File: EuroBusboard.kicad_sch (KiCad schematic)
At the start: 24 parts, among them J1 Power In, J10 IDC5, J11 JST5, J12 IDC6, J13 JST6, J14 IDC7, J15 JST7, J16 IDC8, J17 JST8, J18 Power thru, J2 IDC1, J3 JST1, J4 IDC2, J5 JST2, J6 IDC3, J7 JST3, J8 IDC4, J9 JST4

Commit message: Schematic rev0.1 update
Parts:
- added D3, D4: 4007, symbol Device:D
- added H1, H2, H3, H4: MountingHole_Pad, symbol Mechanical:MountingHole_Pad
- added J19: Power In, symbol DIYSynthMNL:JST_Eurorack_power_3P
- added J20: Power thru, symbol DIYSynthMNL:JST_Eurorack_power_3P
- added TP1: +12V, symbol Connector:TestPoint
- added TP2: GND, symbol Connector:TestPoint
- added TP3: -12V, symbol Connector:TestPoint
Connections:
- net +12V: now also D3.1 (K), J20.1 (+12v), TP1.1; no longer J1.1 (Pin_1)
- net -12V: now also D4.2 (A), J20.3 (-12v), TP3.1; no longer J1.3 (Pin_3)
- net GND: now also H1.1, H2.1, H3.1, H4.1, J19.2 (GND), J20.2 (GND), TP2.1
- new net +12V_IN: D3.2 (A), J1.1 (Pin_1), J19.1 (+12v)
- new net -12V_IN: D4.1 (K), J1.3 (Pin_3), J19.3 (-12v)
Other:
- moved on the sheet: C1, C2, D1, D2, J1, J10, J11, J12, J13, J14, J15, J16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

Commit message: PCB finished
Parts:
- added H5, H6: MountingHole_Pad, DIYSynthMNL:MountingHole_M3_Standoff_Pad, symbol Mechanical:MountingHole_Pad
- added J21: Power Thru, DIYSynthMNL:IDC-Header_2x05_P2.54mm_Vertical_BigPads, symbol DIYSynthMNL:EURO_PWR_2x5
- added J22: Power In, DIYSynthMNL:IDC-Header_2x05_P2.54mm_Vertical_BigPads, symbol DIYSynthMNL:EURO_PWR_2x5
- C1, C2: footprint (none) -> Capacitor_THT:CP_Radial_D8.0mm_P3.50mm
- D1, D2: footprint (none) -> DIYSynthMNL:LED_D5.0mm_BigPads
- D3, D4: footprint (none) -> DIYSynthMNL:D_DO-41_SOD81_P7.62mm_Horizontal_BigPads
- H1, H2, H3, H4: footprint (none) -> DIYSynthMNL:MountingHole_M3_Standoff_Pad
- J1, J18: footprint (none) -> DIYSynthMNL:TerminalBlock_MetzConnect_Type101_RT01603HBWC_1x03_P5.08mm_Horizontal
- J10, J12, J14, J16, J2, J4, J6, J8: footprint (none) -> DIYSynthMNL:IDC-Header_2x05_P2.54mm_Vertical_BigPads
- J11, J13, J15, J17, J19, J20, J3, J5, J7, J9: footprint (none) -> DIYSynthMNL:Eurorack_power_jst_3P
- R1, R2: footprint (none) -> DIYSynthMNL:R_quarter_watt_L6.3mm_D2.5mm_P7.62mm
- TP1, TP2, TP3: footprint (none) -> TestPoint:TestPoint_THTPad_2.0x2.0mm_Drill1.0mm
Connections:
- net GND is gone; now on net +12V: C1.2, C2.1, D2.2 (A), H1.1, H2.1, H3.1, H4.1, J1.2 (Pin_2), J10.3 (GND), J10.4 (GND), J10.5 (GND), J10.6 (GND), J10.7 (GND), J10.8 (GND), J11.2 (GND), J12.3 (GND), J12.4 (GND), J12.5 (GND), J12.6 (GND), J12.7 (GND), J12.8 (GND), J13.2 (GND), J14.3 (GND), J14.4 (GND), J14.5 (GND), J14.6 (GND), J14.7 (GND), J14.8 (GND), J15.2 (GND), J16.3 (GND), J16.4 (GND), J16.5 (GND), J16.6 (GND), J16.7 (GND), J16.8 (GND), J17.2 (GND), J18.2 (Pin_2), J19.2 (GND), J2.3 (GND), J2.4 (GND), J2.5 (GND), J2.6 (GND), J2.7 (GND), J2.8 (GND), J20.2 (GND), J3.2 (GND), J4.3 (GND), J4.4 (GND), J4.5 (GND), J4.6 (GND), J4.7 (GND), J4.8 (GND), J5.2 (GND), J6.3 (GND), J6.4 (GND), J6.5 (GND), J6.6 (GND), J6.7 (GND), J6.8 (GND), J7.2 (GND), J8.3 (GND), J8.4 (GND), J8.5 (GND), J8.6 (GND), J8.7 (GND), J8.8 (GND), J9.2 (GND), R1.1, TP2.1
- net +12V: now also H5.1, H6.1, J21.10 (+12V), J21.3 (GND), J21.4 (GND), J21.5 (GND), J21.6 (GND), J21.7 (GND), J21.8 (GND), J21.9 (+12V), J22.3 (GND), J22.4 (GND), J22.5 (GND), J22.6 (GND), J22.7 (GND), J22.8 (GND)
- net +12V_IN: now also J22.10 (+12V), J22.9 (+12V)
- net -12V: now also J21.1 (-12V), J21.2 (-12V)
- net -12V_IN: now also J22.1 (-12V), J22.2 (-12V)

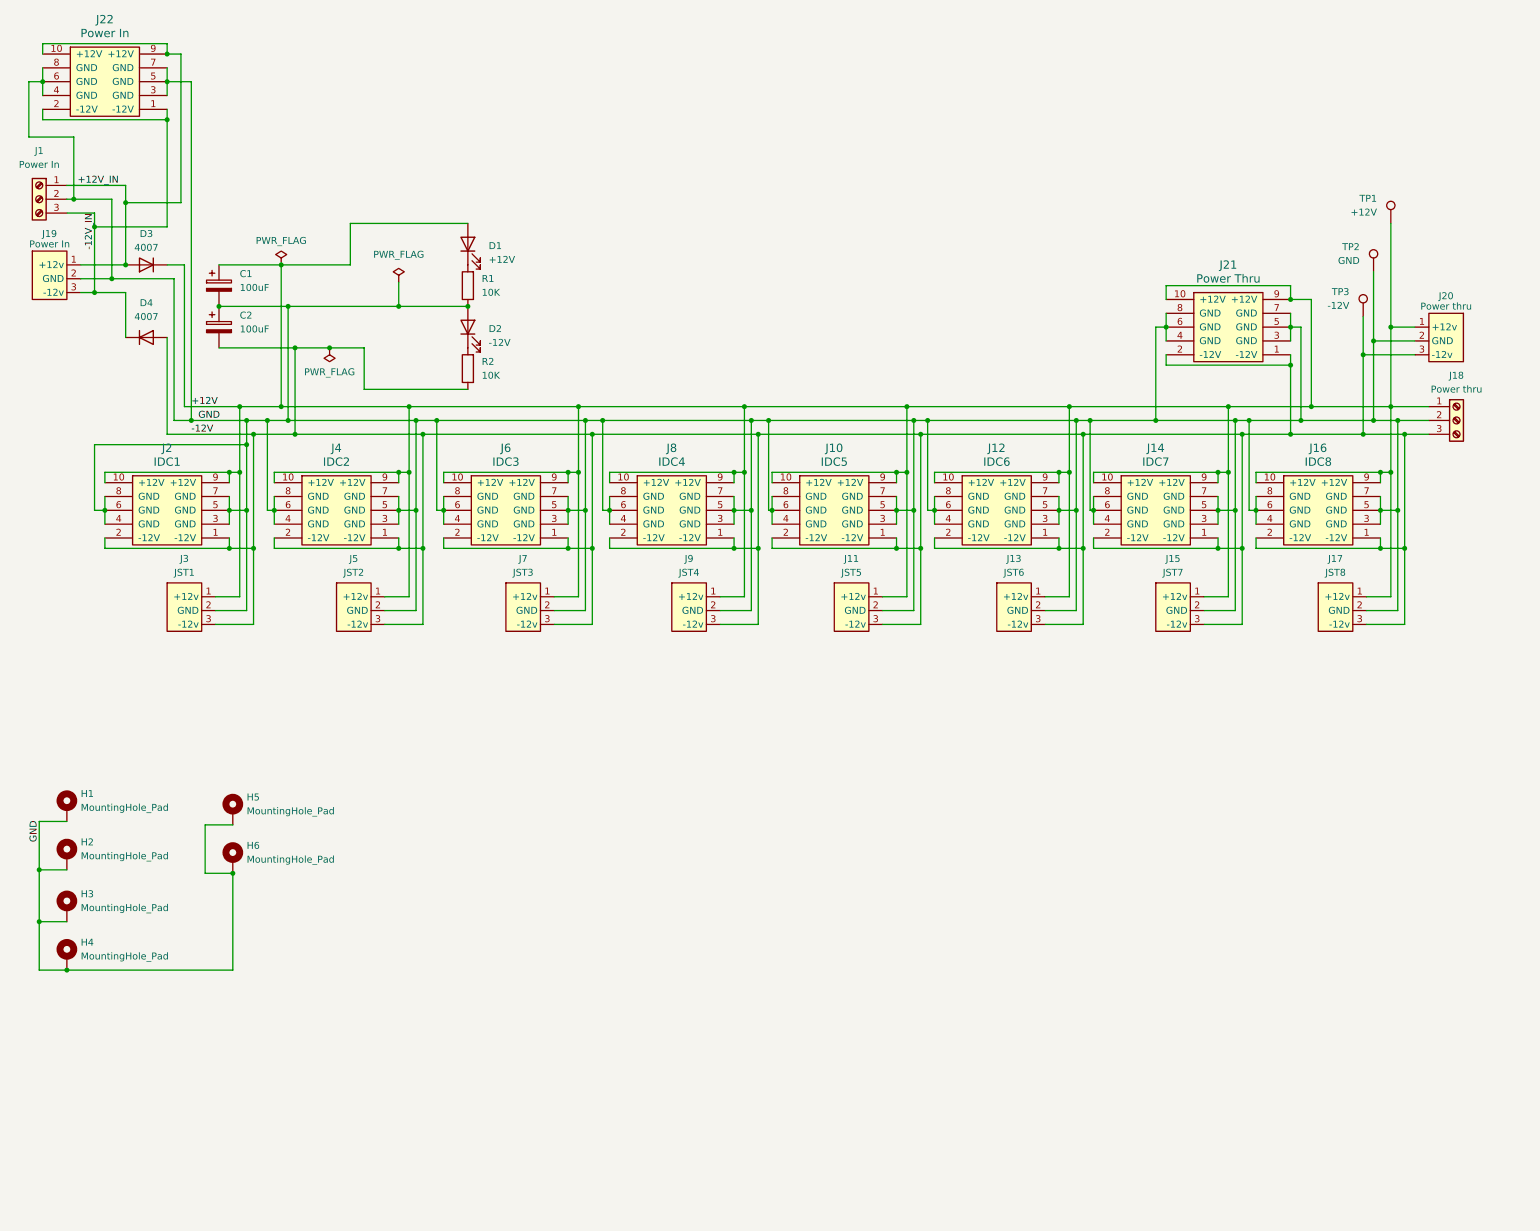
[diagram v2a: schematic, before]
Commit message: added idc and jst only bus boards
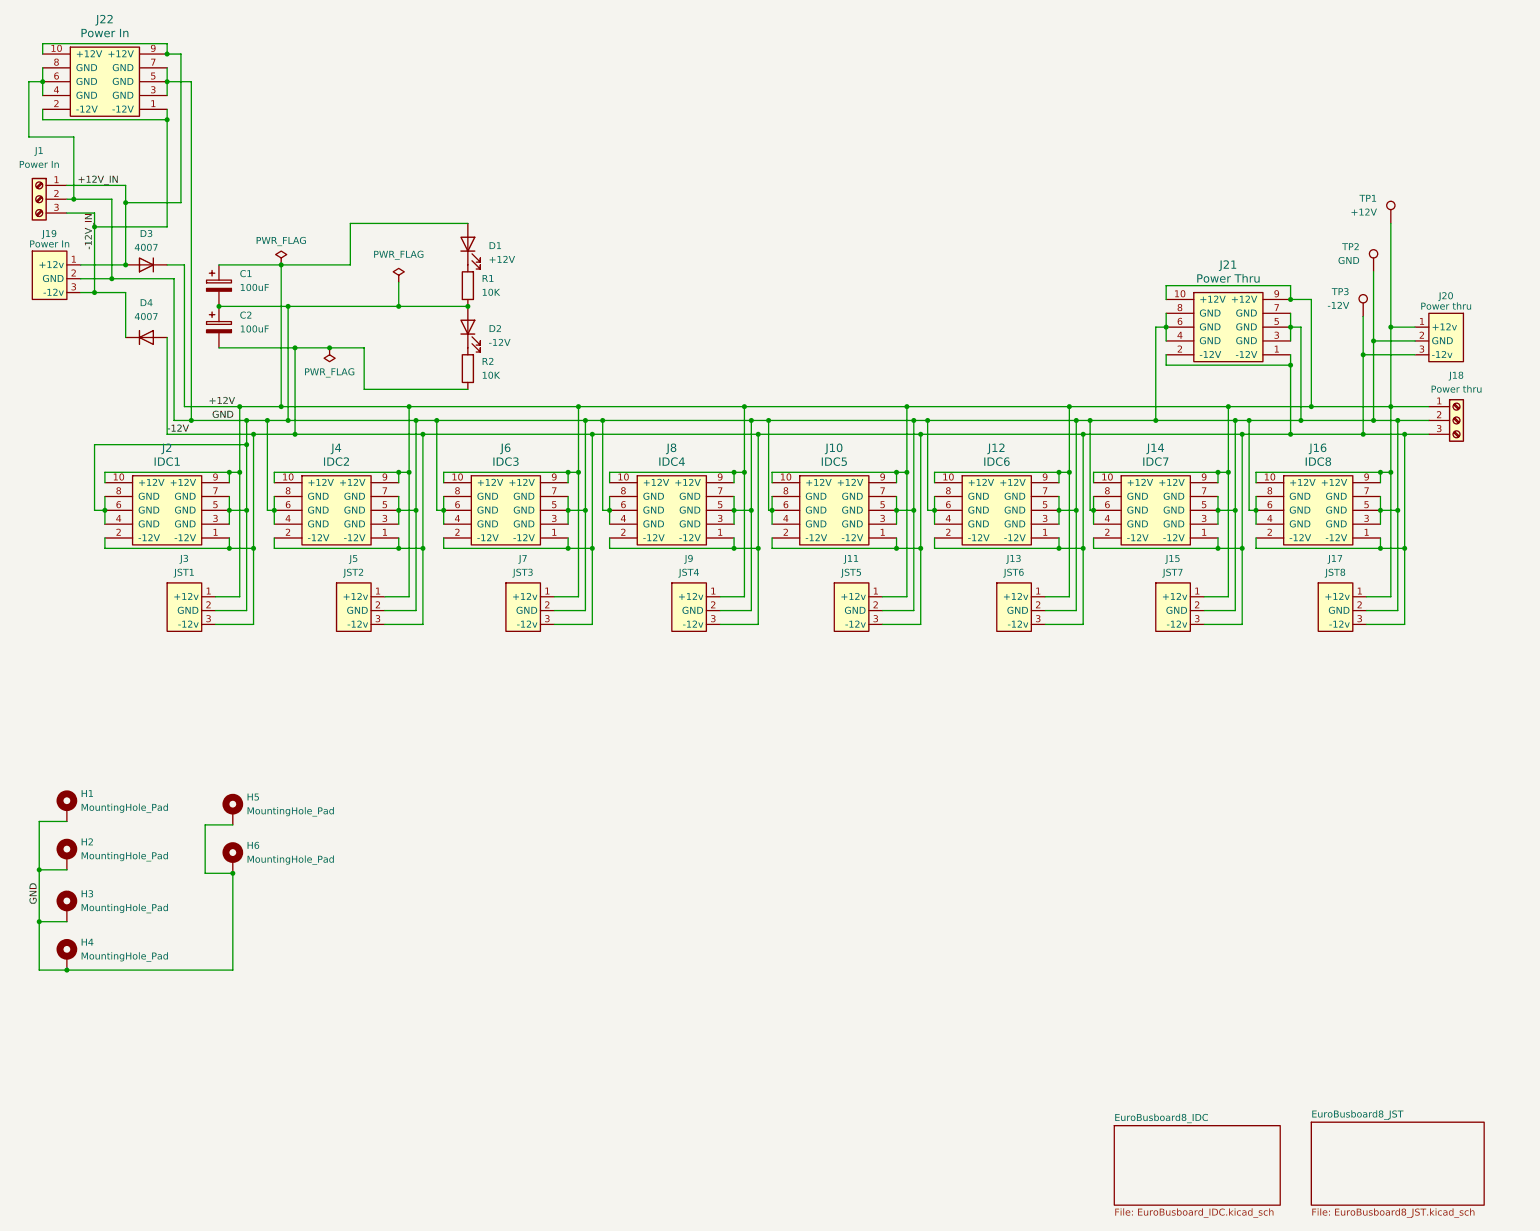
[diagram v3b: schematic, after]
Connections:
- net +12V: no longer C1.2, C2.1, D2.2 (A), H1.1, H2.1, H3.1, H4.1, H5.1, H6.1, J1.2 (Pin_2), J10.3 (GND), J10.4 (GND), J10.5 (GND), J10.6 (GND), J10.7 (GND), J10.8 (GND), J11.2 (GND), J12.3 (GND), J12.4 (GND), J12.5 (GND), J12.6 (GND), J12.7 (GND), J12.8 (GND), J13.2 (GND), J14.3 (GND), J14.4 (GND), J14.5 (GND), J14.6 (GND), J14.7 (GND), J14.8 (GND), J15.2 (GND), J16.3 (GND), J16.4 (GND), J16.5 (GND), J16.6 (GND), J16.7 (GND), J16.8 (GND), J17.2 (GND), J18.2 (Pin_2), J19.2 (GND), J2.3 (GND), J2.4 (GND), J2.5 (GND), J2.6 (GND), J2.7 (GND), J2.8 (GND), J20.2 (GND), J21.3 (GND), J21.4 (GND), J21.5 (GND), J21.6 (GND), J21.7 (GND), J21.8 (GND), J22.3 (GND), J22.4 (GND), J22.5 (GND), J22.6 (GND), J22.7 (GND), J22.8 (GND), J3.2 (GND), J4.3 (GND), J4.4 (GND), J4.5 (GND), J4.6 (GND), J4.7 (GND), J4.8 (GND), J5.2 (GND), J6.3 (GND), J6.4 (GND), J6.5 (GND), J6.6 (GND), J6.7 (GND), J6.8 (GND), J7.2 (GND), J8.3 (GND), J8.4 (GND), J8.5 (GND), J8.6 (GND), J8.7 (GND), J8.8 (GND), J9.2 (GND), R1.1, TP2.1
- new net GND: C1.2, C2.1, D2.2 (A), H1.1, H2.1, H3.1, H4.1, H5.1, H6.1, J1.2 (Pin_2), J10.3 (GND), J10.4 (GND), J10.5 (GND), J10.6 (GND), J10.7 (GND), J10.8 (GND), J11.2 (GND), J12.3 (GND), J12.4 (GND), J12.5 (GND), J12.6 (GND), J12.7 (GND), J12.8 (GND), J13.2 (GND), J14.3 (GND), J14.4 (GND), J14.5 (GND), J14.6 (GND), J14.7 (GND), J14.8 (GND), J15.2 (GND), J16.3 (GND), J16.4 (GND), J16.5 (GND), J16.6 (GND), J16.7 (GND), J16.8 (GND), J17.2 (GND), J18.2 (Pin_2), J19.2 (GND), J2.3 (GND), J2.4 (GND), J2.5 (GND), J2.6 (GND), J2.7 (GND), J2.8 (GND), J20.2 (GND), J21.3 (GND), J21.4 (GND), J21.5 (GND), J21.6 (GND), J21.7 (GND), J21.8 (GND), J22.3 (GND), J22.4 (GND), J22.5 (GND), J22.6 (GND), J22.7 (GND), J22.8 (GND), J3.2 (GND), J4.3 (GND), J4.4 (GND), J4.5 (GND), J4.6 (GND), J4.7 (GND), J4.8 (GND), J5.2 (GND), J6.3 (GND), J6.4 (GND), J6.5 (GND), J6.6 (GND), J6.7 (GND), J6.8 (GND), J7.2 (GND), J8.3 (GND), J8.4 (GND), J8.5 (GND), J8.6 (GND), J8.7 (GND), J8.8 (GND), J9.2 (GND), R1.1, TP2.1
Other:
- added sheet EuroBusboard8_IDC (EuroBusboard_IDC.kicad_sch)
- added sheet EuroBusboard8_JST (EuroBusboard8_JST.kicad_sch)
- title: EuroBusboard8 -> EuroBusboard8_IDC_JST
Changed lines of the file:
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@@
   (paper "A4")
   (title_block
-    (title "EuroBusboard8")
+    (title "EuroBusboard8_IDC_JST")
     (date "2024-01-01")
     (rev "0.1")
@@
     (effects (font (size 1.27 1.27)) (justify right bottom))
   )
-  (label "-12V" (at 46.99 93.98 0) (fields_autoplaced)
+  (label "-12V" (at 42.545 93.98 0) (fields_autoplaced)
     (effects (font (size 1.27 1.27)) (justify left bottom))
   )
-  (label "GND" (at 48.26 91.44 0) (fields_autoplaced)
+  (label "GND" (at 50.8 91.44 0) (fields_autoplaced)
     (effects (font (size 1.27 1.27)) (justify left bottom))
   )
-  (label "GND" (at 19.05 168.91 90) (fields_autoplaced)
+  (label "GND" (at 19.05 180.34 90) (fields_autoplaced)
     (effects (font (size 1.27 1.27)) (justify left bottom))
   )
-  (label "+12V" (at 46.99 88.9 0) (fields_autoplaced)
+  (label "+12V" (at 50.165 88.9 0) (fields_autoplaced)
     (effects (font (size 1.27 1.27)) (justify left bottom))
   )
@@
     )
   )
-  (symbol (lib_id "DIYSynthMNL:EURO_PWR_2x5") (at 194.945 107.95 0) (unit 1)
+  (symbol (lib_name "EURO_PWR_2x5_9") (lib_id "DIYSynthMNL:EURO_PWR_2x5") (at 194.945 107.95 0) (unit 1)
     (in_bom yes) (on_board yes) (dnp no) (fields_autoplaced)
     (property "Reference" "J12" (at 194.945 96.52 0)
@@
     )
   )
-  (symbol (lib_id "DIYSynthMNL:EURO_PWR_2x5") (at 73.66 107.95 0) (unit 1)
+  (symbol (lib_name "EURO_PWR_2x5_6") (lib_id "DIYSynthMNL:EURO_PWR_2x5") (at 73.66 107.95 0) (unit 1)
     (in_bom yes) (on_board yes) (dnp no) (fields_autoplaced)
     (property "Reference" "J4" (at 73.66 96.52 0)
@@
     )
   )
-  (symbol (lib_id "DIYSynthMNL:JST_Eurorack_power_3P") (at 111.125 121.285 0) (unit 1)
+  (symbol (lib_name "JST_Eurorack_power_3P_5") (lib_id "DIYSynthMNL:JST_Eurorack_power_3P") (at 111.125 121.285 0) (unit 1)
     (in_bom yes) (on_board yes) (dnp no) (fields_autoplaced)
     (property "Reference" "J7" (at 107.95 116.84 0)
@@
     )
   )
-  (symbol (lib_id "DIYSynthMNL:EURO_PWR_2x5") (at 165.1 107.95 0) (unit 1)
+  (symbol (lib_name "EURO_PWR_2x5_8") (lib_id "DIYSynthMNL:EURO_PWR_2x5") (at 165.1 107.95 0) (unit 1)
     (in_bom yes) (on_board yes) (dnp no) (fields_autoplaced)
     (property "Reference" "J10" (at 165.1 96.52 0)
@@
     )
   )
-  (symbol (lib_id "DIYSynthMNL:EURO_PWR_2x5") (at 42.545 107.95 0) (unit 1)
+  (symbol (lib_name "EURO_PWR_2x5_5") (lib_id "DIYSynthMNL:EURO_PWR_2x5") (at 42.545 107.95 0) (unit 1)
     (in_bom yes) (on_board yes) (dnp no)
     (property "Reference" "J2" (at 42.545 96.52 0)
@@
     )
   )
-  (symbol (lib_id "DIYSynthMNL:JST_Eurorack_power_3P") (at 24.13 60.325 0) (unit 1)
+  (symbol (lib_name "JST_Eurorack_power_3P_8") (lib_id "DIYSynthMNL:JST_Eurorack_power_3P") (at 24.13 60.325 0) (unit 1)
     (in_bom yes) (on_board yes) (dnp no)
     (property "Reference" "J19" (at 20.955 57.15 0)
@@
     )
   )
-  (symbol (lib_id "DIYSynthMNL:EURO_PWR_2x5") (at 31.115 29.21 0) (unit 1)
+  (symbol (lib_name "EURO_PWR_2x5_7") (lib_id "DIYSynthMNL:EURO_PWR_2x5") (at 31.115 29.21 0) (unit 1)
     (in_bom yes) (on_board yes) (dnp no) (fields_autoplaced)
     (property "Reference" "J22" (at 31.115 17.78 0)
@@
     )
   )
-  (symbol (lib_id "DIYSynthMNL:JST_Eurorack_power_3P") (at 274.32 71.755 0) (mirror y) (unit 1)
+  (symbol (lib_name "JST_Eurorack_power_3P_4") (lib_id "DIYSynthMNL:JST_Eurorack_power_3P") (at 274.32 71.755 0) (mirror y) (unit 1)
     (in_bom yes) (on_board yes) (dnp no)
     (property "Reference" "J20" (at 277.495 68.58 0)
@@
     )
   )
-  (symbol (lib_id "DIYSynthMNL:JST_Eurorack_power_3P") (at 80.01 121.285 0) (unit 1)
+  (symbol (lib_name "JST_Eurorack_power_3P_3") (lib_id "DIYSynthMNL:JST_Eurorack_power_3P") (at 80.01 121.285 0) (unit 1)
     (in_bom yes) (on_board yes) (dnp no) (fields_autoplaced)
     (property "Reference" "J5" (at 76.835 116.84 0)
@@
     )
   )
-  (symbol (lib_id "DIYSynthMNL:EURO_PWR_2x5") (at 224.155 107.95 0) (unit 1)
+  (symbol (lib_name "EURO_PWR_2x5_4") (lib_id "DIYSynthMNL:EURO_PWR_2x5") (at 224.155 107.95 0) (unit 1)
     (in_bom yes) (on_board yes) (dnp no) (fields_autoplaced)
     (property "Reference" "J14" (at 224.155 96.52 0)
@@
     )
   )
-  (symbol (lib_id "DIYSynthMNL:JST_Eurorack_power_3P") (at 260.35 121.285 0) (unit 1)
+  (symbol (lib_name "JST_Eurorack_power_3P_9") (lib_id "DIYSynthMNL:JST_Eurorack_power_3P") (at 260.35 121.285 0) (unit 1)
     (in_bom yes) (on_board yes) (dnp no) (fields_autoplaced)
     (property "Reference" "J17" (at 257.175 116.84 0)
@@
     )
   )
-  (symbol (lib_id "DIYSynthMNL:EURO_PWR_2x5") (at 254 107.95 0) (unit 1)
+  (symbol (lib_name "EURO_PWR_2x5_3") (lib_id "DIYSynthMNL:EURO_PWR_2x5") (at 254 107.95 0) (unit 1)
     (in_bom yes) (on_board yes) (dnp no) (fields_autoplaced)
     (property "Reference" "J16" (at 254 96.52 0)
@@
     )
   )
-  (symbol (lib_id "DIYSynthMNL:EURO_PWR_2x5") (at 135.255 107.95 0) (unit 1)
+  (symbol (lib_name "EURO_PWR_2x5_2") (lib_id "DIYSynthMNL:EURO_PWR_2x5") (at 135.255 107.95 0) (unit 1)
     (in_bom yes) (on_board yes) (dnp no) (fields_autoplaced)
     (property "Reference" "J8" (at 135.255 96.52 0)
@@
     )
   )
-  (symbol (lib_id "DIYSynthMNL:JST_Eurorack_power_3P") (at 48.895 121.285 0) (unit 1)
+  (symbol (lib_name "JST_Eurorack_power_3P_6") (lib_id "DIYSynthMNL:JST_Eurorack_power_3P") (at 48.895 121.285 0) (unit 1)
     (in_bom yes) (on_board yes) (dnp no) (fields_autoplaced)
     (property "Reference" "J3" (at 45.72 116.84 0)
@@
     )
   )
-  (symbol (lib_id "DIYSynthMNL:JST_Eurorack_power_3P") (at 171.45 121.285 0) (unit 1)
+  (symbol (lib_name "JST_Eurorack_power_3P_7") (lib_id "DIYSynthMNL:JST_Eurorack_power_3P") (at 171.45 121.285 0) (unit 1)
     (in_bom yes) (on_board yes) (dnp no) (fields_autoplaced)
     (property "Reference" "J11" (at 168.275 116.84 0)
@@
     )
   )
-  (symbol (lib_id "DIYSynthMNL:EURO_PWR_2x5") (at 104.775 107.95 0) (unit 1)
+  (symbol (lib_name "EURO_PWR_2x5_1") (lib_id "DIYSynthMNL:EURO_PWR_2x5") (at 104.775 107.95 0) (unit 1)
     (in_bom yes) (on_board yes) (dnp no) (fields_autoplaced)
     (property "Reference" "J6" (at 104.775 96.52 0)
@@
     )
   )
-  (symbol (lib_id "DIYSynthMNL:JST_Eurorack_power_3P") (at 201.295 121.285 0) (unit 1)
+  (symbol (lib_name "JST_Eurorack_power_3P_2") (lib_id "DIYSynthMNL:JST_Eurorack_power_3P") (at 201.295 121.285 0) (unit 1)
     (in_bom yes) (on_board yes) (dnp no) (fields_autoplaced)
     (property "Reference" "J13" (at 198.12 116.84 0)
@@
     )
   )
-  (symbol (lib_id "DIYSynthMNL:JST_Eurorack_power_3P") (at 141.605 121.285 0) (unit 1)
+  (symbol (lib_name "JST_Eurorack_power_3P_1") (lib_id "DIYSynthMNL:JST_Eurorack_power_3P") (at 141.605 121.285 0) (unit 1)
     (in_bom yes) (on_board yes) (dnp no) (fields_autoplaced)
     (property "Reference" "J9" (at 138.43 116.84 0)
@@
       )
     )
+  )
+  (sheet (at 216.535 220.98) (size 30.48 14.605) (fields_autoplaced)
+    (stroke (width 0.1524) (type solid))
+    (fill (color 0 0 0 0.0000))
+    (property "Sheetname" "EuroBusboard8_IDC" (at 216.535 220.2684 0)
+      (effects (font (size 1.27 1.27)) (justify left bottom))
+    )
+    (property "Sheetfile" "EuroBusboard_IDC.kicad_sch" (at 216.535 236.1696 0)
+      (effects (font (size 1.27 1.27)) (justify left top))
+    )
+    (instances
+      (project "EuroBusboard"
+        (path "/9225e1c5-5b65-40f1-85db-81016ace963e" (page "2"))
+      )
+    )
+  )
+  (sheet (at 252.73 220.345) (size 31.75 15.24) (fields_autoplaced)
+    (stroke (width 0.1524) (type solid))
+    (fill (color 0 0 0 0.0000))
+    (property "Sheetname" "EuroBusboard8_JST" (at 252.73 219.6334 0)
+      (effects (font (size 1.27 1.27)) (justify left bottom))
+    )
+    (property "Sheetfile" "EuroBusboard8_JST.kicad_sch" (at 252.73 236.1696 0)
+      (effects (font (size 1.27 1.27)) (justify left top))
+    )
+    (instances
+      (project "EuroBusboard"
+        (path "/9225e1c5-5b65-40f1-85db-81016ace963e" (page "3"))
+      )
+    )
